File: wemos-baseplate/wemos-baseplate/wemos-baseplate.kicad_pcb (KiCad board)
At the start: 4 copper layers, 138 x 55 mm, 18 parts, among them J1 Conn_02x16_Odd_Even, J10 Conn_01x04, J11 Conn_01x04, J12 Conn_01x04, J13 Conn_01x04, J14 Conn_01x04, J15 Conn_01x04, J2 Conn_02x16_Odd_Even, J3 Conn_01x04, J4 Conn_01x04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

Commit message: forgotten files
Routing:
- net /GND: track 290.1 -> 20.8 mm
- net /3.3V: track 267.8 -> 101.2 mm
- added copper zone on F.Cu, net /3.3V
- removed copper zone on F.Cu, net /GND

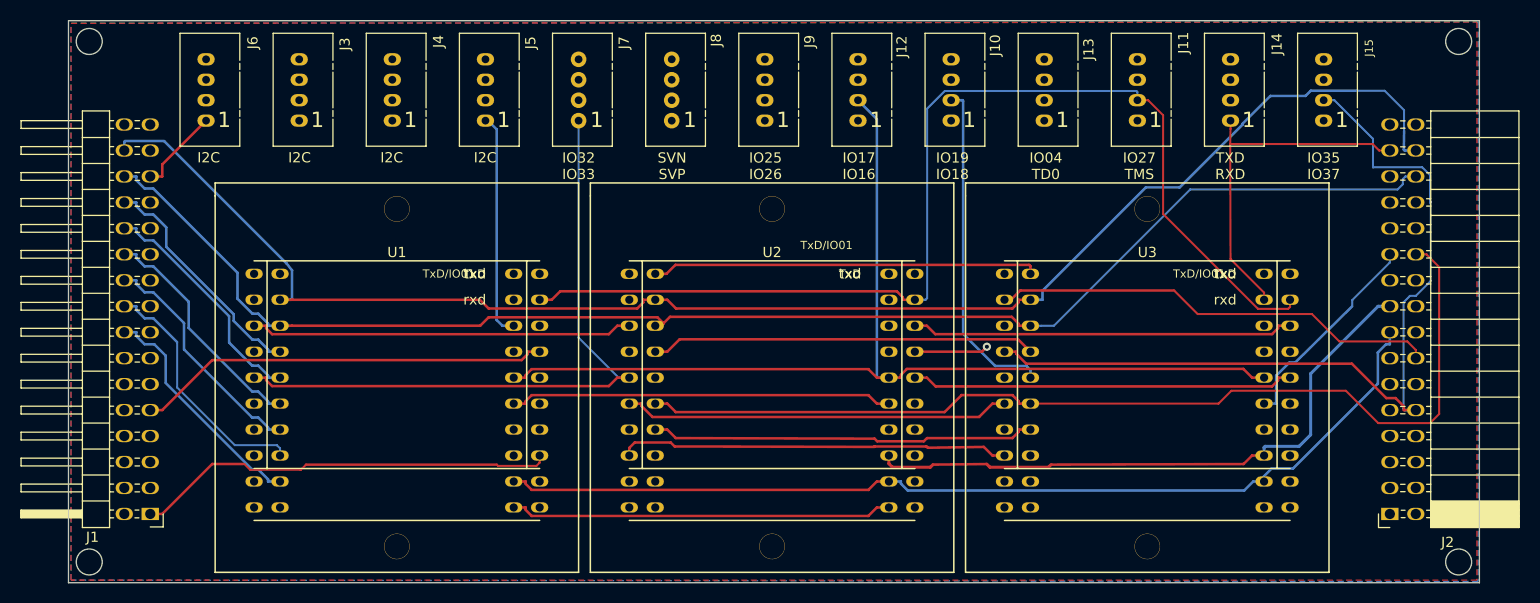
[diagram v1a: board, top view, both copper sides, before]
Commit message: added filled zone for +5V
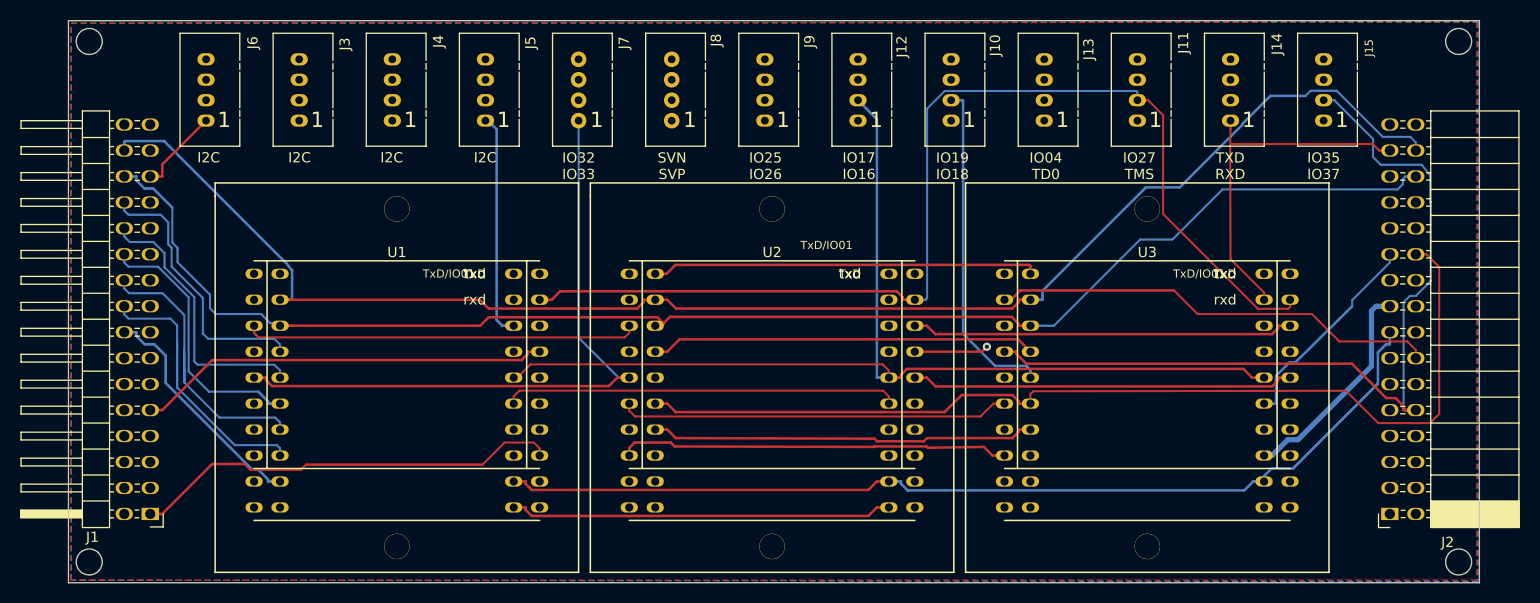
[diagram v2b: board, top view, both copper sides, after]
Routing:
- net /5V: track 166.8 -> 180.3 mm
- net /3.3V: track 101.2 -> 90.0 mm
- net /IO05: track 157.8 -> 163.3 mm
- net /TMS: track 171.5 -> 175.2 mm
- net /IO23: track 158.3 -> 161.8 mm
- net /IO19: track 205.3 -> 208.9 mm
- net /SDA: track 191.0 -> 187.5 mm
- net /IO18: track 201.9 -> 205.3 mm
- net /IO34: track 190.7 -> 188.6 mm
- net /NC2: track 136.6 -> 138.7 mm
- net /IO26: track 168.0 -> 170.0 mm
- net /SVN: track 164.2 -> 166.1 mm
- net /SVP: track 172.1 -> 170.3 mm
- net /IO16: track 170.8 -> 171.8 mm
- net /IO02: track 130.0 -> 130.9 mm
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- added copper zone on In1.Cu, net /5V

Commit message: gnd en 3v3 panes in center now
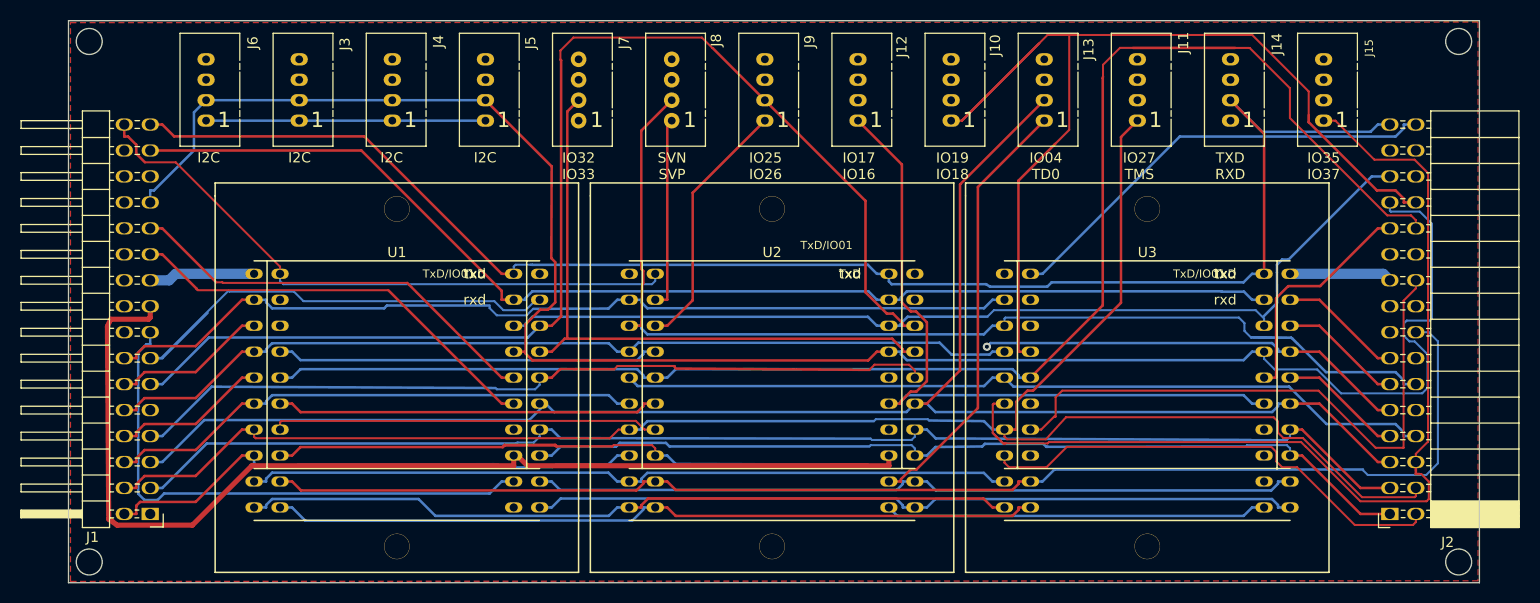
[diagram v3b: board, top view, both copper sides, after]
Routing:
- added copper zone on In1.Cu, net /3.3V
- added copper zone on F.Cu, net /5V
- added copper zone on In2.Cu, net /GND
- removed copper zone on F.Cu, net /3.3V
- removed copper zone on In1.Cu, net /5V
- removed copper zone on B.Cu, net /GND
